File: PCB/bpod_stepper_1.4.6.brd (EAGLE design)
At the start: 83.8 x 63.5 mm, 33 parts, among them IC1 LM3480-5.0, IC2 SN65HVD31DR, IC3 MCP1792, IC4 MCP1793_SOT223-5, J8 POWER_JACK

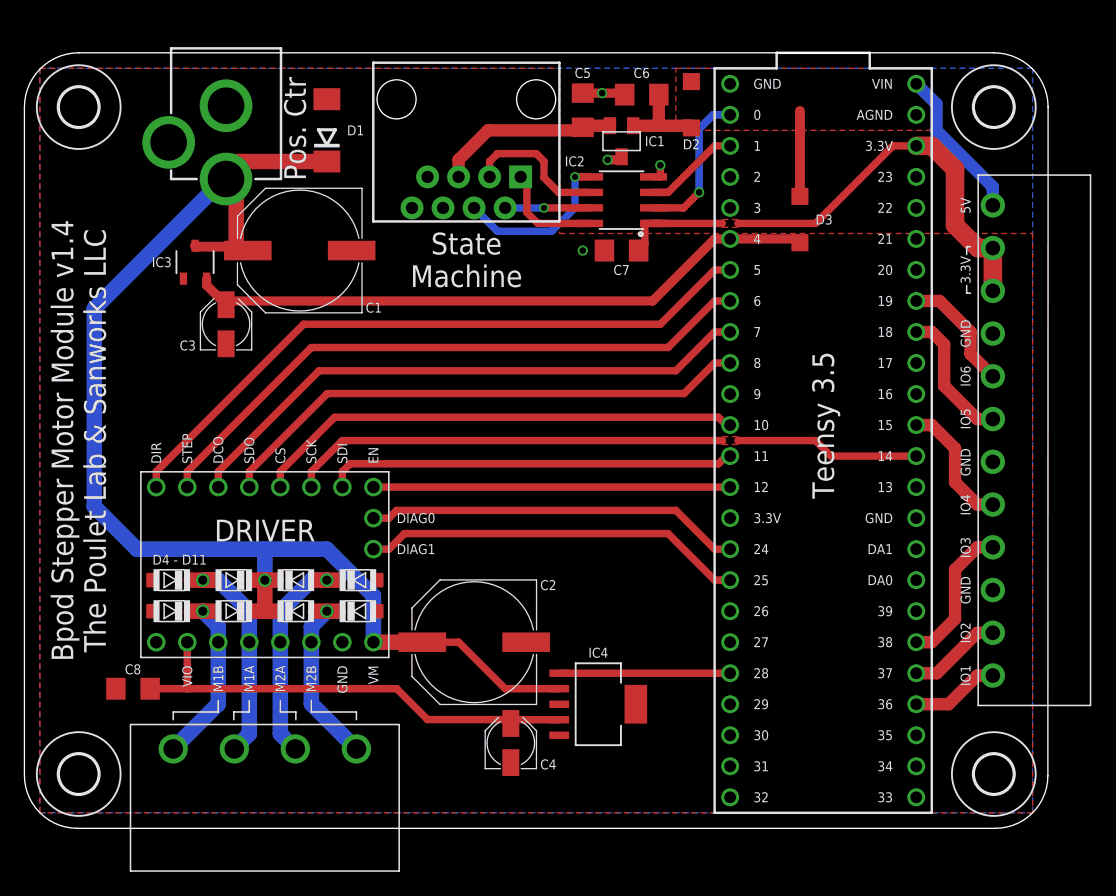
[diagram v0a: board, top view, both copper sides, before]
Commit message: added D12 to prevent current flowing from pin 28 to pin 4
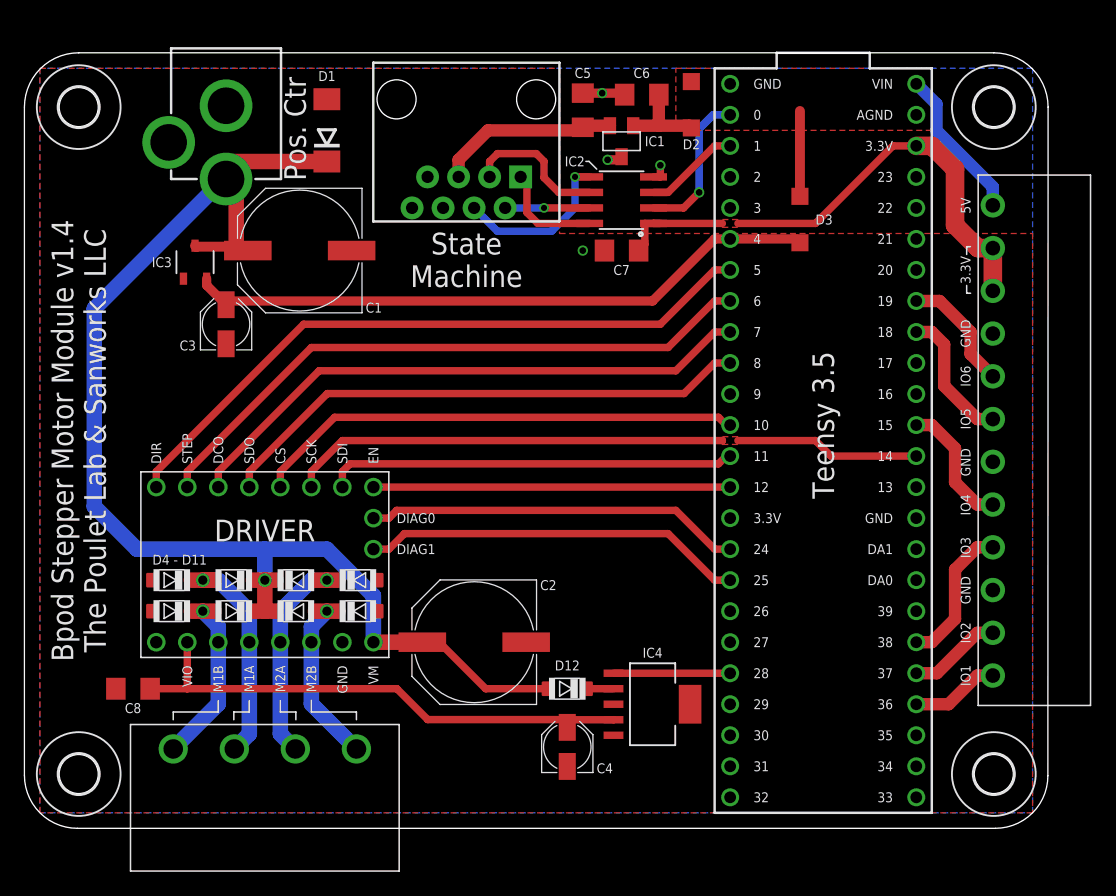
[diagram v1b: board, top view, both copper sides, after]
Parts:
- added D12: S310FA, we-rcl:SOD123
- IC4: value MCP1793_SOT223-5 -> MCP1793
- moved C4 4.63 mm to (44.5, 6.67)
- moved IC4 4.45 mm to (51.4, 10.2)
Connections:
- new net N$1: D12.C, IC4.2
- net VMOTOR: now also D12.A; no longer IC4.2
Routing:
- net VIO: track 38.7 -> 44.1 mm
- net VIO_CTRL: track 14.0 -> 9.55 mm
- net VMOTOR: track 111.0 -> 106.9 mm
- net N$1: track 0.00 -> 2.18 mm
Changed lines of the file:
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@@
 <wire x1="23.495" y1="9.525" x2="23.495" y2="10.4775" width="0.127" layer="25"/>
 <text x="21.2725" y="53.0225" size="1.778" layer="21" font="vector" rot="R90" align="top-left">Pos. Ctr</text>
-<wire x1="45.974" y1="54.61" x2="46.228" y2="54.61" width="0.127" layer="125"/>
-<wire x1="46.228" y1="54.61" x2="46.863" y2="53.975" width="0.127" layer="125"/>
+<wire x1="45.974" y1="54.61" x2="46.228" y2="54.61" width="0.127" layer="21"/>
+<wire x1="46.228" y1="54.61" x2="46.863" y2="53.975" width="0.127" layer="21"/>
 </plain>
 <attributes>
@@
 <element name="U$2" library="SparkFun" package="RJ45-8" value="RJ45-8PTH" x="36.185" y="59.69" smashed="yes" rot="R180"/>
 <element name="D1" library="diode" package="DO214AA" value="" x="24.765" y="57.15" smashed="yes" rot="R90">
-<attribute name="NAME" x="27.1145" y="57.15" size="0.8128" layer="25" font="vector" rot="R180" align="center"/>
+<attribute name="NAME" x="24.765" y="61.595" size="0.8128" layer="25" font="vector" rot="R180" align="center"/>
 <attribute name="VALUE" x="29.376" y="54.51" size="1.27" layer="27" ratio="10" rot="R90"/>
 </element>
@@
 </element>
 <element name="C8" library="SparkFun-Capacitors" package="1206@1" value="100nf" x="8.89" y="11.43" smashed="yes" rot="R180">
-<attribute name="NAME" x="8.89" y="13.0175" size="0.8128" layer="25" font="vector" rot="R180" align="center"/>
+<attribute name="NAME" x="8.89" y="9.8425" size="0.8128" layer="25" font="vector" rot="R180" align="center"/>
 </element>
 <element name="D3" library="diode" package="SOD123" value="MBR0520LT" x="63.5" y="49.8475" smashed="yes" rot="R270">
@@
 <attribute name="VALUE" x="13.97" y="46.355" size="0.4064" layer="27" font="vector" ratio="9" align="center"/>
 </element>
-<element name="IC4" library="MCP1793" package="SOT223-5" value="MCP1793_SOT223-5" x="46.99" y="10.16" smashed="yes" rot="R270">
-<attribute name="NAME" x="46.99" y="13.97" size="0.8128" layer="25" font="vector" align="bottom-center"/>
-<attribute name="VALUE" x="46.7995" y="10.16" size="0.4064" layer="27" font="vector" rot="R270" align="bottom-center"/>
-</element>
-<element name="C4" library="rcl" library_urn="urn:adsk.eagle:library:334" package="PANASONIC_B" package3d_urn="urn:adsk.eagle:package:23421/2" value="" x="39.8272" y="6.985" smashed="yes" rot="R90">
-<attribute name="NAME" x="42.2275" y="4.826" size="0.8128" layer="25" font="vector"/>
-<attribute name="POPULARITY" value="4" x="39.8272" y="6.985" size="1.778" layer="27" rot="R90" display="off"/>
-<attribute name="SPICEPREFIX" value="C" x="39.8272" y="6.985" size="1.778" layer="27" rot="R90" display="off"/>
-<attribute name="VALUE" x="43.1022" y="4.835" size="1.016" layer="27" rot="R90"/>
+<element name="IC4" library="MCP1793" package="SOT223-5" value="MCP1793" x="51.435" y="10.16" smashed="yes" rot="R270">
+<attribute name="NAME" x="51.435" y="13.97" size="0.8128" layer="25" font="vector" align="bottom-center"/>
+<attribute name="VALUE" x="51.2445" y="10.16" size="0.4064" layer="27" font="vector" rot="R270" align="bottom-center"/>
+</element>
+<element name="C4" library="rcl" library_urn="urn:adsk.eagle:library:334" package="PANASONIC_B" package3d_urn="urn:adsk.eagle:package:23421/2" value="" x="44.45" y="6.6675" smashed="yes" rot="R90">
+<attribute name="NAME" x="46.8503" y="4.5085" size="0.8128" layer="25" font="vector"/>
+<attribute name="POPULARITY" value="4" x="44.45" y="6.6675" size="1.778" layer="27" rot="R90" display="off"/>
+<attribute name="SPICEPREFIX" value="C" x="44.45" y="6.6675" size="1.778" layer="27" rot="R90" display="off"/>
+<attribute name="VALUE" x="47.725" y="4.5175" size="1.016" layer="27" rot="R90"/>
 </element>
 <element name="C3" library="rcl" library_urn="urn:adsk.eagle:library:334" package="PANASONIC_B" package3d_urn="urn:adsk.eagle:package:23421/2" value="" x="16.51" y="41.275" smashed="yes" rot="R90">
@@
 <attribute name="SPICEPREFIX" value="C" x="16.51" y="41.275" size="1.778" layer="27" rot="R90" display="off"/>
 <attribute name="VALUE" x="19.785" y="39.125" size="1.016" layer="27" rot="R90"/>
+</element>
+<element name="D12" library="we-rcl" package="SOD123" value="S310FA" x="44.45" y="11.43" smashed="yes" rot="R270">
+<attribute name="NAME" x="44.45" y="13.335" size="0.8128" layer="25" font="vector" rot="R180" align="center"/>
 </element>
 </elements>
@@
 <wire x1="20.625" y1="20.32" x2="19.685" y2="20.32" width="1.27" layer="1"/>
 <wire x1="31.75" y1="15.24" x2="28.575" y2="15.24" width="1.27" layer="1"/>
-<wire x1="31.7375" y1="15.24" x2="31.75" y2="15.24" width="0.6096" layer="1"/>
-<wire x1="31.7375" y1="15.24" x2="32.58" y2="15.24" width="1.27" layer="1"/>
-<wire x1="43.7896" y1="11.43" x2="39.37" y2="11.43" width="0.6096" layer="1"/>
-<wire x1="39.37" y1="11.43" x2="35.56" y2="15.24" width="0.6096" layer="1"/>
-<wire x1="35.56" y1="15.24" x2="28.575" y2="15.24" width="0.6096" layer="1"/>
+<wire x1="31.75" y1="15.24" x2="32.58" y2="15.24" width="1.27" layer="1"/>
+<wire x1="33.96" y1="15.24" x2="31.75" y2="15.24" width="0.6096" layer="1"/>
 <wire x1="9.2075" y1="22.86" x2="5.715" y2="26.3525" width="1.27" layer="16"/>
 <contactref element="J8" pad="PWR"/>
@@
 <wire x1="13.97" y1="47.705" x2="14.05" y2="47.625" width="0.8128" layer="1"/>
 <wire x1="17.34" y1="47.625" x2="14.05" y2="47.625" width="0.8128" layer="1"/>
-<contactref element="IC4" pad="2"/>
+<contactref element="D12" pad="A"/>
+<wire x1="42.85" y1="11.43" x2="37.77" y2="11.43" width="0.6096" layer="1"/>
+<wire x1="37.77" y1="11.43" x2="33.96" y2="15.24" width="0.6096" layer="1"/>
 </signal>
 <signal name="EN">
@@
 <contactref element="IC4" pad="4"/>
 <contactref element="C4" pad="+"/>
-<wire x1="30.48" y1="11.4325" x2="13.335" y2="11.4325" width="0.6096" layer="1"/>
-<wire x1="10.29" y1="11.43" x2="10.2925" y2="11.4325" width="0.762" layer="1"/>
-<wire x1="10.2925" y1="11.4325" x2="10.605" y2="11.4325" width="0.762" layer="1"/>
-<wire x1="39.8272" y1="8.585" x2="39.6875" y2="8.9025" width="0.6096" layer="1"/>
-<wire x1="39.6875" y1="8.9025" x2="33.01" y2="8.9025" width="0.6096" layer="1"/>
-<wire x1="33.01" y1="8.9025" x2="30.48" y2="11.4325" width="0.6096" layer="1"/>
-<wire x1="39.8272" y1="8.585" x2="40.31" y2="8.89" width="0.6096" layer="1"/>
-<wire x1="43.7896" y1="8.89" x2="40.31" y2="8.89" width="0.6096" layer="1"/>
+<wire x1="10.605" y1="11.4325" x2="10.2925" y2="11.4325" width="0.762" layer="1"/>
+<wire x1="10.2925" y1="11.4325" x2="10.29" y2="11.43" width="0.762" layer="1"/>
+<wire x1="48.2346" y1="8.89" x2="48.233846875" y2="8.9025" width="0.6096" layer="1"/>
+<wire x1="33.02" y1="8.9025" x2="30.49" y2="11.4325" width="0.6096" layer="1"/>
+<wire x1="13.335" y1="11.4325" x2="30.49" y2="11.4325" width="0.6096" layer="1"/>
+<wire x1="48.2346" y1="8.89" x2="44.45" y2="8.89" width="0.6096" layer="1"/>
+<wire x1="44.45" y1="8.2675" x2="44.45" y2="8.89" width="0.6096" layer="1"/>
+<wire x1="44.45" y1="8.2675" x2="44.45" y2="8.9025" width="0.6096" layer="1"/>
+<wire x1="44.45" y1="8.9025" x2="33.02" y2="8.9025" width="0.6096" layer="1"/>
 </signal>
 <signal name="VIO_CTRL">
 <contactref element="IC4" pad="1"/>
 <contactref element="TEENSY" pad="28"/>
-<wire x1="43.7896" y1="12.7" x2="57.785" y2="12.7" width="0.6096" layer="1"/>
+<wire x1="57.785" y1="12.7" x2="48.2346" y2="12.7" width="0.6096" layer="1"/>
 </signal>
 <signal name="BOOL_VM">
@@
 <contactref element="TEENSY" pad="AGND"/>
 </signal>
+<signal name="N$1">
+<contactref element="D12" pad="C"/>
+<contactref element="IC4" pad="2"/>
+<wire x1="46.05" y1="11.43" x2="48.2346" y2="11.43" width="0.6096" layer="1"/>
+</signal>
 </signals>
